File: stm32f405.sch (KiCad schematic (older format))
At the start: 17 parts, among them Q1 CRYSTAL_50X32, U1 STM32_STM32F10XRXT6

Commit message: added lots of stuff
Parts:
- removed U1: STM32_STM32F10XRXT6, Housings_QFP:LQFP-64_10x10mm_Pitch0.5mm, symbol STM32_STM32F10XRXT6
- added U1: STM32F405R, Housings_QFP:LQFP-64_10x10mm_Pitch0.5mm, symbol STM32F405R
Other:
- moved on the sheet: C1, C10, C11, C12, C2, C3, C4, C5, C6, C7, C8, C9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

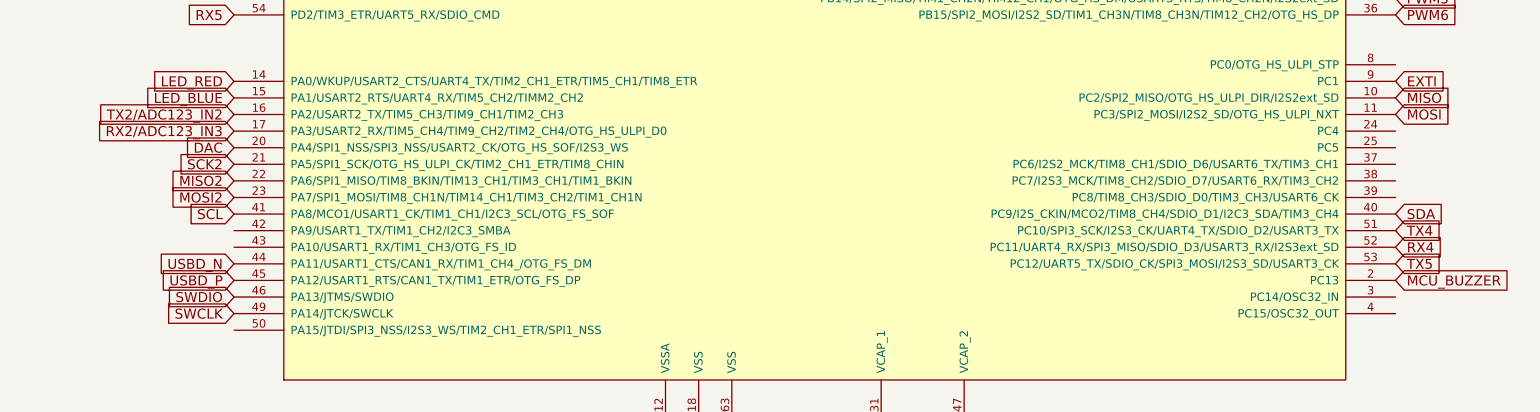
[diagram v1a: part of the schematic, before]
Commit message: added IMU int and USB sense in schematic
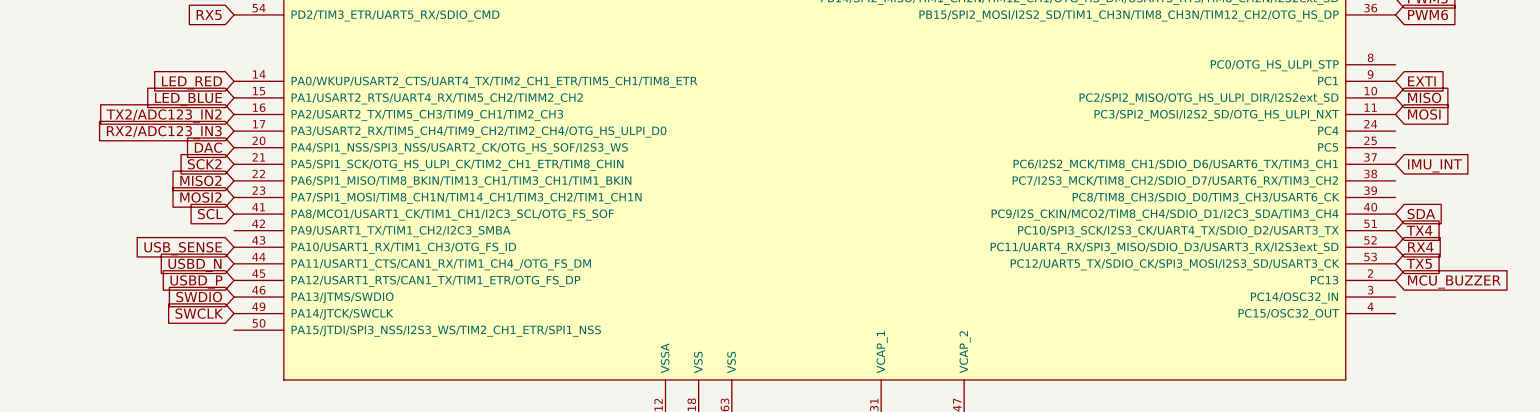
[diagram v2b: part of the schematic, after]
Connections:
- net IMU_INT: now reaches U1.37 (PC6/I2S2_MCK/TIM8_CH1/SDIO_D6/USART6_TX/TIM3_CH1)
- net USB_SENSE: now reaches U1.43 (PA10/USART1_RX/TIM1_CH3/OTG_FS_ID)
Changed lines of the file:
@@
 	6650 1600 6650 750
 Connection ~ 6650 750
+Text GLabel 9050 4700 2    60   Input ~ 0
+IMU_INT
+Text GLabel 2050 5200 0    60   Input ~ 0
+USB_SENSE
 $EndSCHEMATC

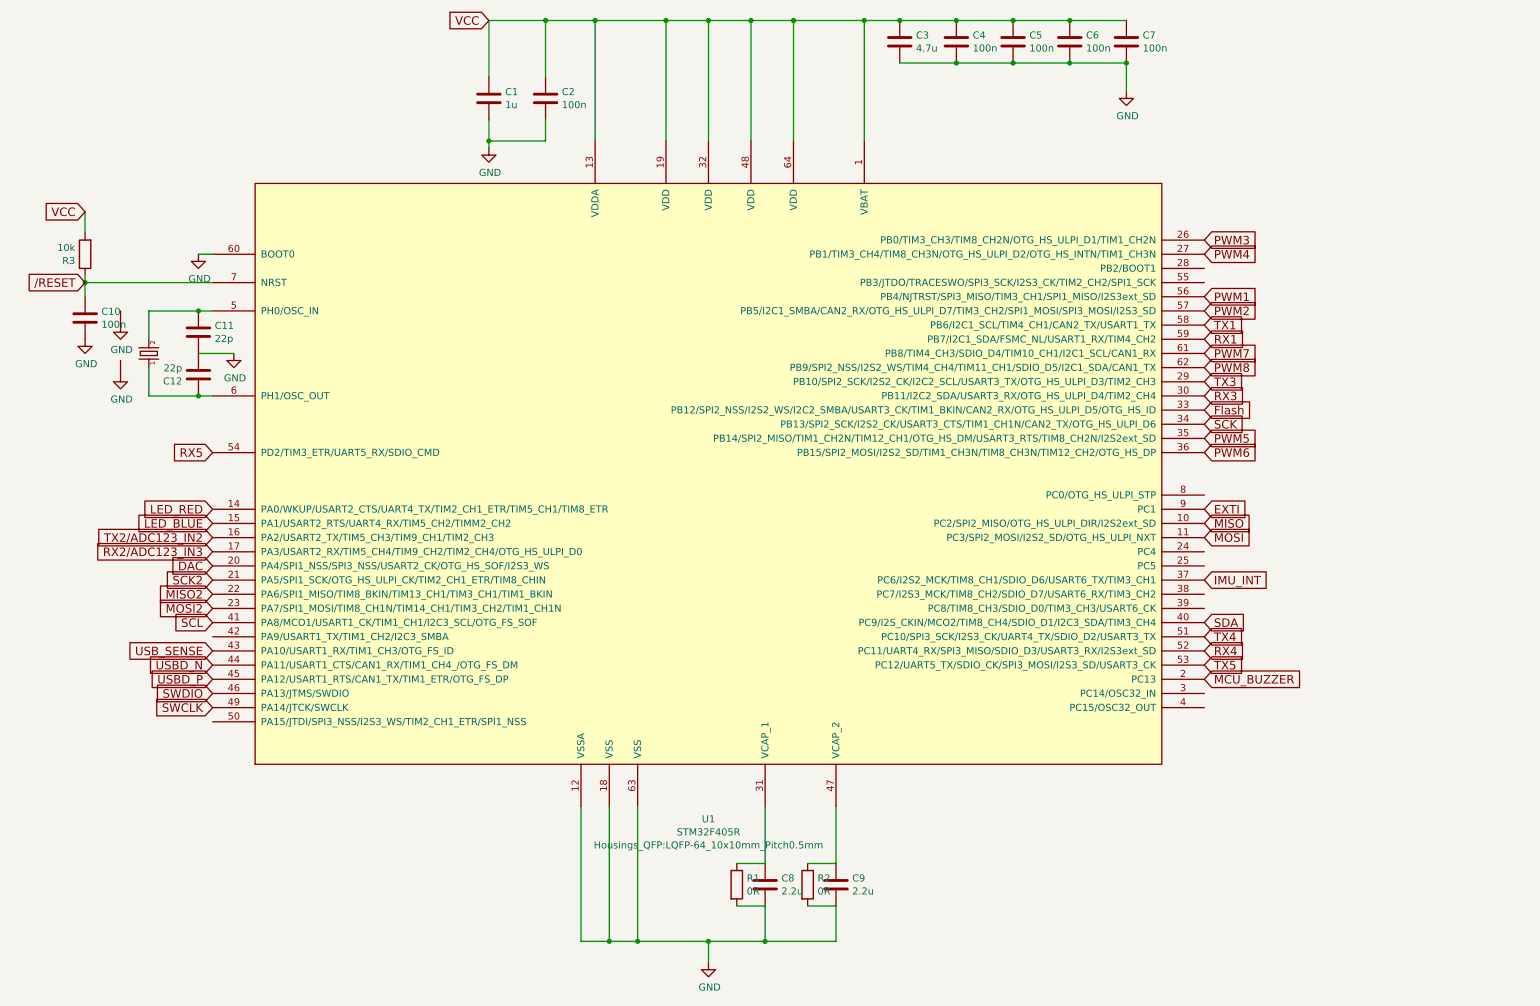
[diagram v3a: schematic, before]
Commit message: changed some netnames
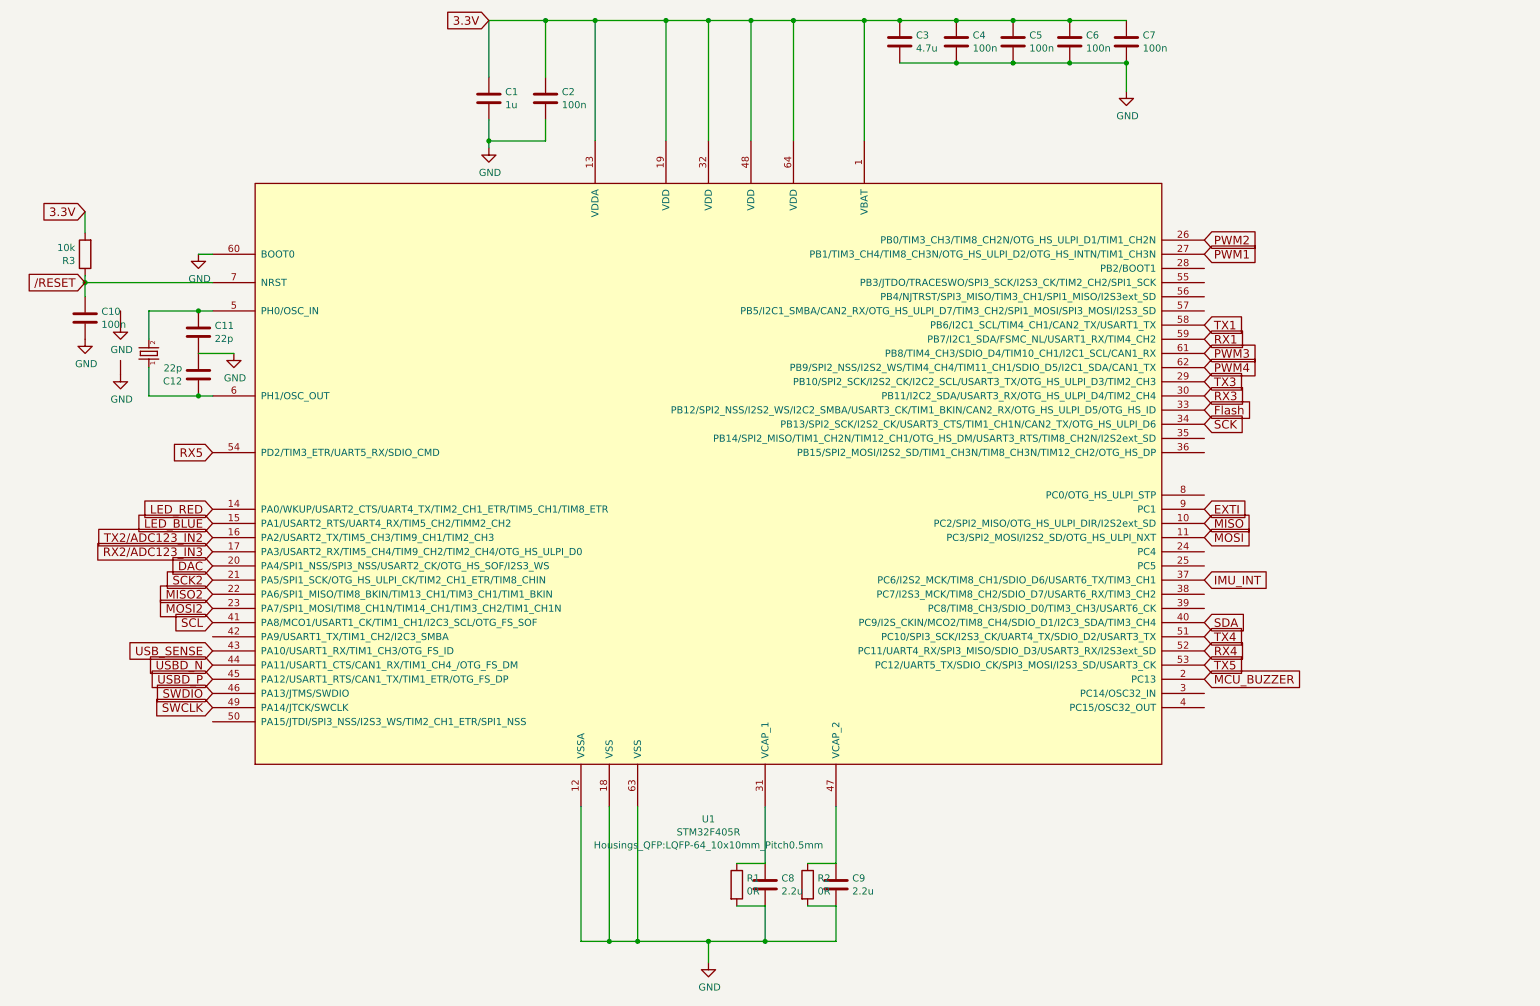
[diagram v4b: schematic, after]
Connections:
- net PWM7 is gone; now on net PWM3: U1.61 (PB8/TIM4_CH3/SDIO_D4/TIM10_CH1/I2C1_SCL/CAN1_RX)
- net PWM8 is gone; now on net PWM4: U1.62 (PB9/SPI2_NSS/I2S2_WS/TIM4_CH4/TIM11_CH1/SDIO_D5/I2C1_SDA/CAN1_TX)
- net PWM1: now also U1.27 (PB1/TIM3_CH4/TIM8_CH3N/OTG_HS_ULPI_D2/OTG_HS_INTN/TIM1_CH3N); no longer U1.56 (PB4/NJTRST/SPI3_MISO/TIM3_CH1/SPI1_MISO/I2S3ext_SD)
- net PWM2: now also U1.26 (PB0/TIM3_CH3/TIM8_CH2N/OTG_HS_ULPI_D1/TIM1_CH2N); no longer U1.57 (PB5/I2C1_SMBA/CAN2_RX/OTG_HS_ULPI_D7/TIM3_CH2/SPI1_MOSI/SPI3_MOSI/I2S3_SD)
- net PWM3: no longer U1.26 (PB0/TIM3_CH3/TIM8_CH2N/OTG_HS_ULPI_D1/TIM1_CH2N)
- net PWM4: no longer U1.27 (PB1/TIM3_CH4/TIM8_CH3N/OTG_HS_ULPI_D2/OTG_HS_INTN/TIM1_CH3N)
- net PWM5: no longer names the net of U1.35 (PB14/SPI2_MISO/TIM1_CH2N/TIM12_CH1/OTG_HS_DM/USART3_RTS/TIM8_CH2N/I2S2ext_SD)
- net PWM6: no longer names the net of U1.36 (PB15/SPI2_MOSI/I2S2_SD/TIM1_CH3N/TIM8_CH3N/TIM12_CH2/OTG_HS_DP)
- net VCC renamed 3.3V
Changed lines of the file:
@@
 Comment4 ""
 $EndDescr
-Text GLabel 9050 3800 2    60   Input ~ 0
-PWM6
-Text GLabel 9050 3700 2    60   Input ~ 0
-PWM5
 Text GLabel 9050 3600 2    60   Input ~ 0
 SCK
@@
 TX3
 Text GLabel 9050 3200 2    60   Input ~ 0
-PWM8
+PWM4
 Text GLabel 9050 3100 2    60   Input ~ 0
-PWM7
+PWM3
 Text GLabel 9050 3000 2    60   Input ~ 0
 RX1
 Text GLabel 9050 2900 2    60   Input ~ 0
 TX1
-Text GLabel 9050 2800 2    60   Input ~ 0
+Text GLabel 9050 2400 2    60   Input ~ 0
+PWM1
+Text GLabel 9050 2300 2    60   Input ~ 0
 PWM2
-Text GLabel 9050 2700 2    60   Input ~ 0
-PWM1
-Text GLabel 9050 2400 2    60   Input ~ 0
-PWM4
-Text GLabel 9050 2300 2    60   Input ~ 0
-PWM3
 $Comp
 L C C4
@@
 $EndComp
 $Comp
-L GND #PWR33
+L GND #PWR016
 U 1 1 569AE259
 P 5550 7400
-F 0 "#PWR33" H 5550 7150 50  0001 C CNN
+F 0 "#PWR016" H 5550 7150 50  0001 C CNN
 F 1 "GND" H 5558 7226 50  0000 C CNN
 F 2 "" H 5550 7400 50  0000 C CNN
@@
 $EndComp
 $Comp
-L GND #PWR3
+L GND #PWR017
 U 1 1 569AE27B
 P 4000 1650
-F 0 "#PWR3" H 4000 1400 50  0001 C CNN
+F 0 "#PWR017" H 4000 1400 50  0001 C CNN
 F 1 "GND" H 4008 1476 50  0000 C CNN
 F 2 "" H 4000 1650 50  0000 C CNN
@@
 $EndComp
 Text GLabel 1150 2100 0    60   Input ~ 0
-VCC
+3.3V
 $Comp
 L R R3
@@
 $EndComp
 $Comp
-L GND #PWR12
+L GND #PWR018
 U 1 1 569AE29F
 P 1150 3000
-F 0 "#PWR12" H 1150 2750 50  0001 C CNN
+F 0 "#PWR018" H 1150 2750 50  0001 C CNN
 F 1 "GND" H 1158 2826 50  0000 C CNN
 F 2 "" H 1150 3000 50  0000 C CNN
@@
 $EndComp
 $Comp
-L GND #PWR11
+L GND #PWR019
 U 1 1 569AE2B7
 P 1400 2900
-F 0 "#PWR11" H 1400 2650 50  0001 C CNN
+F 0 "#PWR019" H 1400 2650 50  0001 C CNN
 F 1 "GND" H 1408 2726 50  0000 C CNN
 F 2 "" H 1400 2900 50  0000 C CNN
@@
 $EndComp
 $Comp
-L GND #PWR15
+L GND #PWR020
 U 1 1 569AE2BD
 P 1400 3250
-F 0 "#PWR15" H 1400 3000 50  0001 C CNN
+F 0 "#PWR020" H 1400 3000 50  0001 C CNN
 F 1 "GND" H 1408 3076 50  0000 C CNN
 F 2 "" H 1400 3250 50  0000 C CNN
@@
 $EndComp
 $Comp
-L GND #PWR13
+L GND #PWR021
 U 1 1 569AE2D1
 P 2200 3100
-F 0 "#PWR13" H 2200 2850 50  0001 C CNN
+F 0 "#PWR021" H 2200 2850 50  0001 C CNN
 F 1 "GND" H 2208 2926 50  0000 C CNN
 F 2 "" H 2200 3100 50  0000 C CNN
@@
 	4000 750  8500 750
 $Comp
-L GND #PWR6
+L GND #PWR022
 U 1 1 569E1F9F
 P 1950 2400
-F 0 "#PWR6" H 1950 2150 50  0001 C CNN
+F 0 "#PWR022" H 1950 2150 50  0001 C CNN
 F 1 "GND" H 1958 2226 50  0000 C CNN
 F 2 "" H 1950 2400 50  0000 C CNN
@@
 	1150 2100 1150 2250
 Text GLabel 4000 750  0    60   Input ~ 0
-VCC
+3.3V
 Wire Wire Line
 	5250 750  5250 1600
@@
 Connection ~ 6900 750
 $Comp
-L GND #PWR1
+L GND #PWR023
 U 1 1 569E5F3D
 P 8500 1250
-F 0 "#PWR1" H 8500 1000 50  0001 C CNN
+F 0 "#PWR023" H 8500 1000 50  0001 C CNN
 F 1 "GND" H 8508 1076 50  0000 C CNN
 F 2 "" H 8500 1250 50  0000 C CNN
